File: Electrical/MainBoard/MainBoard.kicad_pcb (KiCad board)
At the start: 4 copper layers, 100 x 86.3 mm, 137 parts, among them J1 SNAP Program, J13 Refl_PCB_Connect, J14 Refl_PCB_Connect, J15 Refl_PCB_Connect, J16 Conn_02x03_Odd_Even, J17 MEM2061-01-188-00-A, J18 Conn_02x02_Odd_Even, J19 Conn_02x03_Odd_Even, J2 3.3V Supply, J20 Conn_02x03_Odd_Even, J21 Conn_02x03_Odd_Even, J22 Conn_02x02_Odd_Even, J23 Conn_02x03_Odd_Even, J24 Conn_01x04, J3 5V Supply, J4 USB_B_Micro, J5 Battery1, J6 Battery1, J7 GPIO1, J8 Conn_02x04_Odd_Even, J9 USB_B_Micro, M1 Motor_DC, M2 Motor_DC, SW1 Reset, SW10 SW_SPST, SW2 5V Bypass, SW3 All Power Switch, SW4 User_Button, SW5 User_Button, SW6 User_Button, SW7 SW_SPST, SW8 SW_SPST, SW9 SW_SPST, U1 PIC32MZ2048EFH144-I/PL, U10 DRV8842PWPR, U11 Quad_Encoder, U12 Quad_Encoder, U13 DRV8842PWPR, U15 M95M01-DFMN6TP, U2 AP2114HA-3.3TRG1, U3 AP2114HA-3.3TRG1, U4 ICM-42688-P, U5 GSF7002DW, U6 GSF7002DW, U7 GSF7002DW, U8 GSF7002DW, U9 MCP2221A-I_SL

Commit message: Add some final touches
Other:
- board text added: "Matthew Sato Engineering Informatics Group Stanford University Robot Control, Rev 0.1 11/25/2023"
- board text removed: "Matthew Sato Engineering Informatics Group Stanford University Robot Control, Rev 0.1 11/24/2023"
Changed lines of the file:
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@@
   (title_block
     (title "Main Robot Board")
+    (date "2023-11-25")
     (rev "0.1")
     (company "satomm@stanford.edu")
@@
     (property "Supplier 2" "")
     (property "Supplier 2 P/N" "")
+    (property "exclude_from_bom" "")
     (property "ki_description" "Mounting Hole without connection")
     (property "ki_keywords" "mounting hole")
-    (attr exclude_from_pos_files)
+    (attr exclude_from_pos_files exclude_from_bom)
     (fp_text reference "H2" (at 0 -4.2) (layer "F.SilkS") hide
         (effects (font (size 1 1) (thickness 0.15)))
@@
     (property "Supplier 2" "")
     (property "Supplier 2 P/N" "")
+    (property "exclude_from_bom" "")
     (property "ki_description" "Mounting Hole without connection")
     (property "ki_keywords" "mounting hole")
-    (attr exclude_from_pos_files)
+    (attr exclude_from_pos_files exclude_from_bom)
     (fp_text reference "H4" (at 0 -4.2) (layer "F.SilkS") hide
         (effects (font (size 1 1) (thickness 0.15)))
@@
     (property "Supplier 2" "")
     (property "Supplier 2 P/N" "")
+    (property "exclude_from_bom" "")
     (property "ki_description" "Mounting Hole without connection")
     (property "ki_keywords" "mounting hole")
-    (attr exclude_from_pos_files)
+    (attr exclude_from_pos_files exclude_from_bom)
     (fp_text reference "H1" (at 0 -4.2) (layer "F.SilkS") hide
         (effects (font (size 1 1) (thickness 0.15)))
@@
     (property "Supplier 2" "")
     (property "Supplier 2 P/N" "")
+    (property "exclude_from_bom" "")
     (property "ki_description" "Mounting Hole without connection")
     (property "ki_keywords" "mounting hole")
-    (attr exclude_from_pos_files)
+    (attr exclude_from_pos_files exclude_from_bom)
     (fp_text reference "H3" (at 0 -4.2) (layer "F.SilkS") hide
         (effects (font (size 1 1) (thickness 0.15)))
@@
     (effects (font (size 1 1) (thickness 0.15)) (justify left bottom))
   )
-  (gr_text "Matthew Sato\nEngineering Informatics Group\nStanford University\nRobot Control, Rev 0.1\n11/24/2023" (at 181.9 152) (layer "F.SilkS")
+  (gr_text "Matthew Sato\nEngineering Informatics Group\nStanford University\nRobot Control, Rev 0.1\n11/25/2023" (at 181.9 152) (layer "F.SilkS")
     (effects (font (size 1 1) (thickness 0.15)) (justify left bottom))
   )

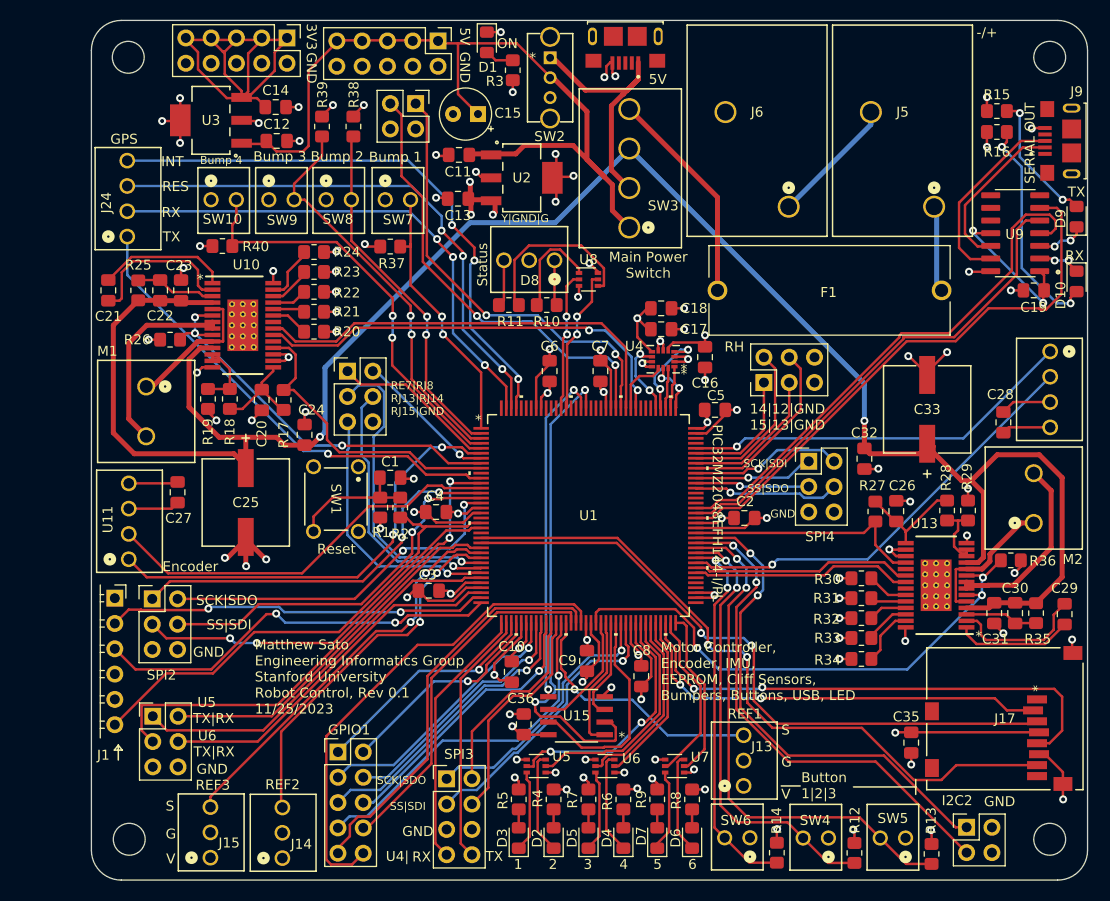
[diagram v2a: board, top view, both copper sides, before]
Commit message: Finish final board design for Rev 0.1 Main board and reflective Sensor. Created Gerbers.
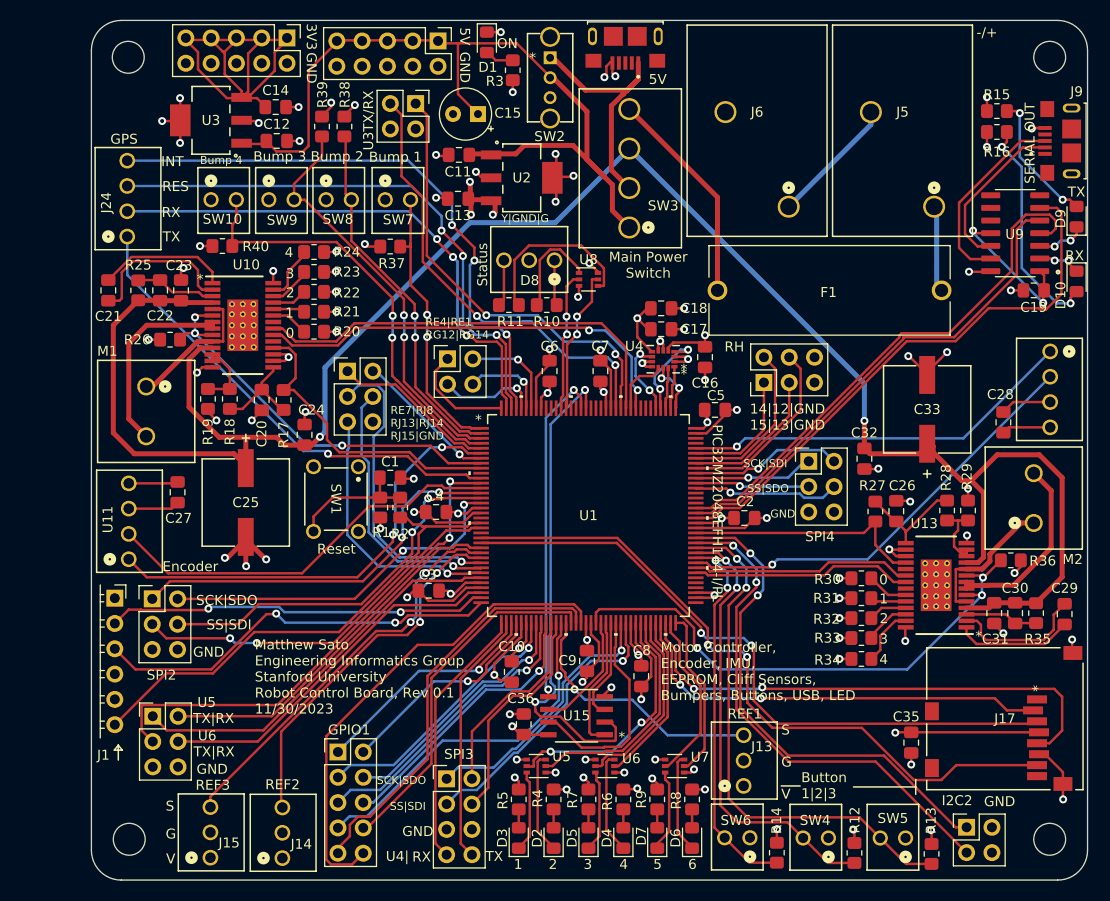
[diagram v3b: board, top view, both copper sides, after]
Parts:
- added J25: Conn_02x02_Odd_Even, Connector_PinHeader_2.54mm:PinHeader_2x02_P2.54mm_Vertical, F.Cu at (201.2, 116.3)
- moved R38 0.90 mm to (190.9, 93.0)
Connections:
- U1 pad 138: unconnected-(U1B-EBID1/PMD1/RE1-Pad138) -> /RE1
- U1 pad 139: unconnected-(U1B-TRD2/SQID2/RG14-Pad139) -> /RG14
- U1 pad 140: unconnected-(U1B-TRD1/SQID1/RG12-Pad140) -> /RG12
- U1 pad 144: unconnected-(U1B-EBID4/AN18/PMD4/RE4-Pad144) -> /RE4
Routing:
- net /RE4: track 0.00 -> 10.9 mm
- net /RG12: track 0.00 -> 10.0 mm, vias 0 -> 1
- net /RE1: track 0.00 -> 9.99 mm, vias 0 -> 1
- net /RG14: track 0.00 -> 8.47 mm, vias 0 -> 1
- net /U2RX: track 52.1 -> 53.5 mm
- net /GPS_INT: track 58.1 -> 59.5 mm
- net /GPS_Reset: track 55.0 -> 56.2 mm
- net /Bump1: track 27.2 -> 28.3 mm
- net /Bump2: track 35.6 -> 36.6 mm
- net /Bump3: track 40.5 -> 41.1 mm
- net /Bump4: track 41.8 -> 42.4 mm
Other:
- board text added: "0"
- board text added: "Matthew Sato Engineering Informatics Group Stanford University Robot Control Board, Rev 0.1 11/30/2023"
- board text added: "RE4|RE1 RG12|RG14"
- board text added: "U3TX/RX"
- board text removed: "Matthew Sato Engineering Informatics Group Stanford University Robot Control, Rev 0.1 11/25/2023"

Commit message: Made V0.2 revisions to Main Board
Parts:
- removed C16: 0.01 uF, Capacitor_SMD:C_0805_2012Metric_Pad1.18x1.45mm_HandSolder
- removed C17: 0.1 uF, Capacitor_SMD:C_0805_2012Metric_Pad1.18x1.45mm_HandSolder
- removed C18: 2.2 uF, Capacitor_SMD:C_0805_2012Metric_Pad1.18x1.45mm_HandSolder
- removed U4: ICM-42688-P, RobotLibrary:LGA14_2P5X3X0P91_TDK-M
- added J26: Conn_02x04_Odd_Even, Connector_PinHeader_2.54mm:PinHeader_2x04_P2.54mm_Vertical, F.Cu at (222.5, 110.4)
- added R47: 0.1R, Resistor_SMD:R_0603_1608Metric_Pad0.98x0.95mm_HandSolder, B.Cu at (170.8, 113.7)
- added R48: 0.05 R, Resistor_SMD:R_0603_1608Metric_Pad0.98x0.95mm_HandSolder, B.Cu at (167.4, 113.7)
- added R49: 0.1R, Resistor_SMD:R_0603_1608Metric_Pad0.98x0.95mm_HandSolder, B.Cu at (260.0, 138.1)
- added R50: 0.05 R, Resistor_SMD:R_0603_1608Metric_Pad0.98x0.95mm_HandSolder, B.Cu at (263.4, 138.1)
- J20: value Conn_02x03_Odd_Even -> Conn_01x06; footprint Connector_PinHeader_2.54mm:PinHeader_2x03_P2.54mm_Vertical -> Connector_Molex:Molex_KK-254_AE-6410-06A_1x06_P2.54mm_Vertical
- R26, R36: value 0.25R -> 0.1R; footprint Resistor_SMD:R_0805_2012Metric_Pad1.20x1.40mm_HandSolder -> Resistor_SMD:R_0603_1608Metric_Pad0.98x0.95mm_HandSolder; moved to B.Cu
- moved J20 2.13 mm to (172.1, 142.4)
- moved R36 1.99 mm to (256.6, 138.1)
- moved R26 1.02 mm to (174.2, 113.7)
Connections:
- J1 pad 1: unconnected-(J1-Pin_1-Pad1) -> Net-(J1-Pin_1)
- J1 pad 2: Net-(J1-Pin_2) -> +3.3V
- J1 pad 3: Net-(J1-Pin_3) -> GND
- J1 pad 4: GND -> Net-(J1-Pin_4)
- J1 pad 5: +3.3V -> Net-(J1-Pin_5)
- J1 pad 6: Net-(J1-Pin_6) -> unconnected-(J1-Pin_6-Pad6)
- J20 pad 2: /SDO2 -> /SS2*
- J20 pad 3: /SS2* -> /SDO2
- R2 pad 1: Net-(J1-Pin_6) -> Net-(J1-Pin_1)
- R26 pad 1: GND -> Net-(R26-Pad1)
- R36 pad 1: GND -> Net-(R36-Pad1)
- U1 pad 20: Net-(J1-Pin_6) -> Net-(J1-Pin_1)
- U1 pad 35: Net-(J1-Pin_2) -> Net-(J1-Pin_5)
- U1 pad 36: Net-(J1-Pin_3) -> Net-(J1-Pin_4)
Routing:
- net Net-(J1-Pin_6): track 49.0 -> 0.00 mm
- net Net-(J1-Pin_5): track 0.00 -> 41.5 mm, vias 0 -> 1
- net Net-(J1-Pin_3): track 41.2 -> 0.00 mm, vias 2 -> 0
- net Net-(J1-Pin_1): track 0.00 -> 40.9 mm, vias 0 -> 1
- net Net-(J1-Pin_4): track 0.00 -> 39.7 mm, vias 0 -> 1
- net Net-(J1-Pin_2): track 38.3 -> 0.00 mm, vias 2 -> 0
- net +3.3V: track 161.9 -> 150.1 mm, vias 42 -> 40
- net GND: track 149.3 -> 138.4 mm, vias 72 -> 66
- net /SS1*: track 5.97 -> 16.2 mm
- net /SDI2: track 38.1 -> 32.2 mm
- net /SCK1: track 5.45 -> 10.1 mm, vias 2 -> 0
- net /SS2*: track 38.6 -> 35.0 mm, vias 2 -> 0
- net /IMU_INT1: track 9.41 -> 6.75 mm, vias 2 -> 0
- net /SDO2: track 36.3 -> 34.1 mm
- net /MotorCurrent2: track 54.1 -> 52.2 mm
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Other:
- board text added: "GND GND"
- board text added: "Matthew Sato, 02/02/2024 Engineering Informatics Group Stanford University Robot Control Board, Rev 0.2"
- board text added: "SCK2"
- board text added: "SDI2"
- board text added: "SDO2"
- board text added: "SS2"
- board text removed: "Matthew Sato Engineering Informatics Group Stanford University Robot Control Board, Rev 0.1 11/30/2023"

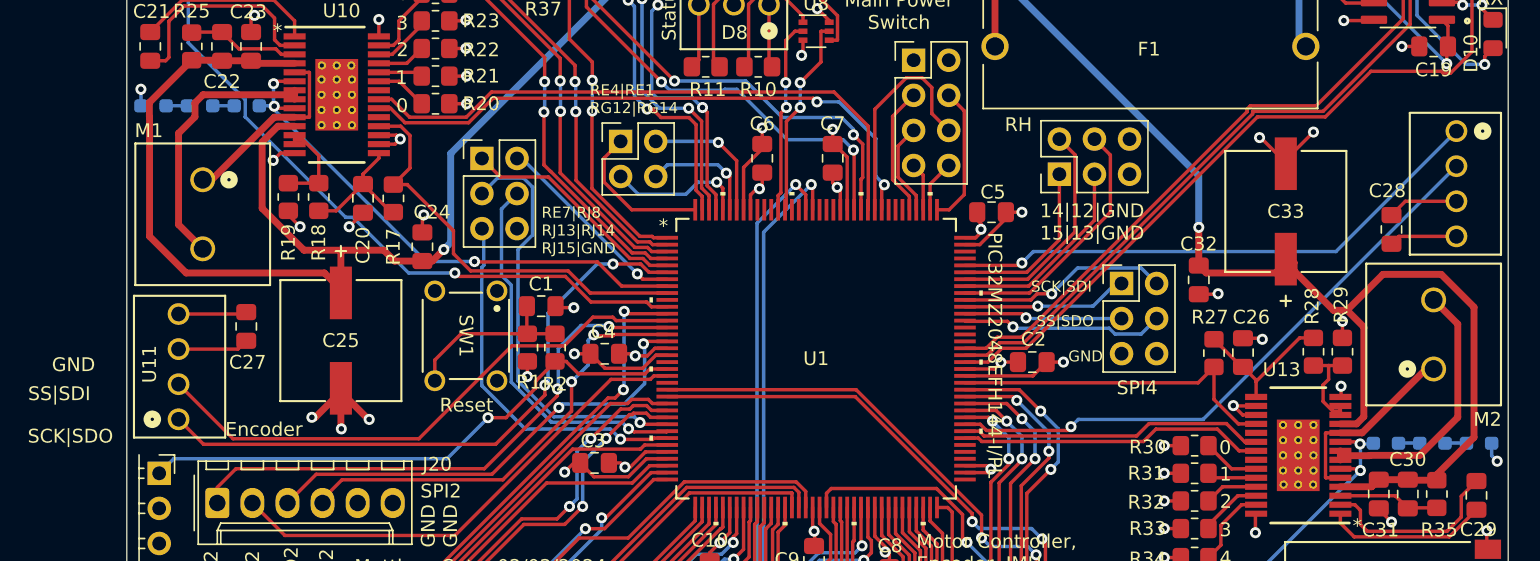
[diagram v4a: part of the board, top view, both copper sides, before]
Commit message: Change molex+terminal block to just 6 position molex for the motor/encoder terminal
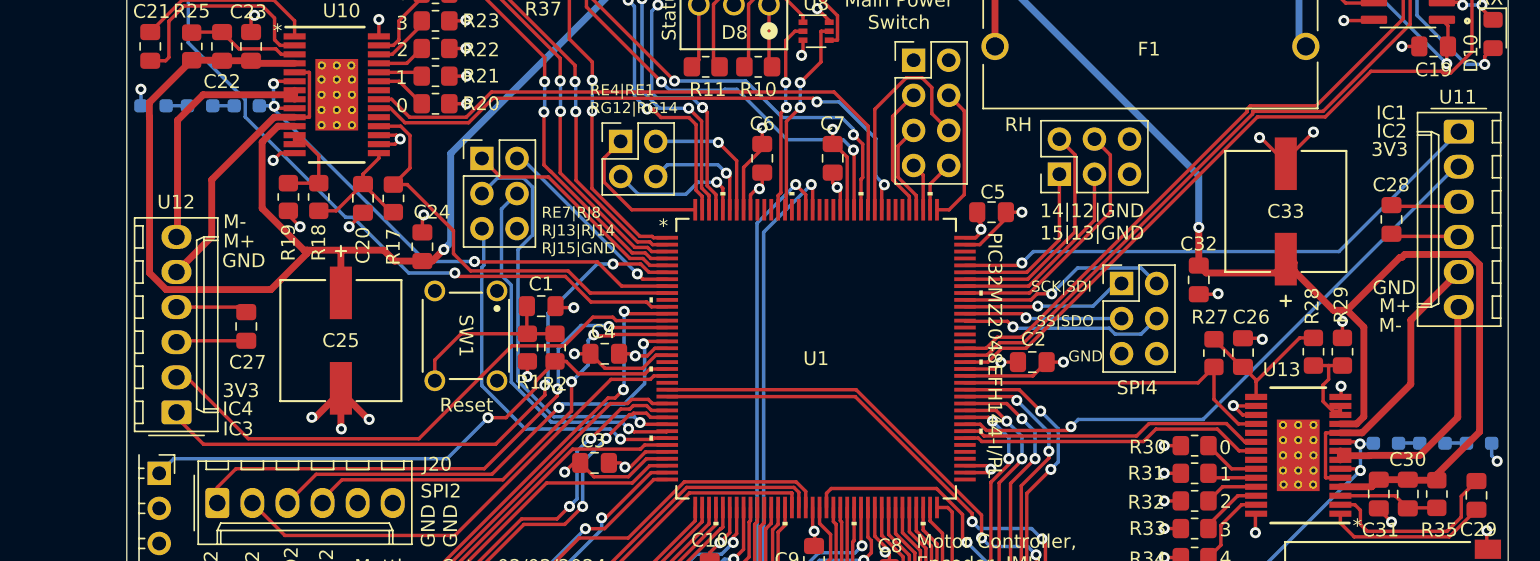
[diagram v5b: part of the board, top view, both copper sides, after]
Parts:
- removed M1, M2: Motor_DC, RobotLibrary:CONN_1890963_PXC
- U11, U12: value Quad_Encoder -> Quad_Encoder_Motor; footprint RobotLibrary:CONN_22-23-2041_MOL -> Connector_Molex:Molex_KK-254_AE-6410-06A_1x06_P2.54mm_Vertical
- moved U11 95.0 mm to (261.9, 115.6), turned to -90 degrees
- moved U12 94.9 mm to (169.1, 135.9), turned to 90 degrees
- moved C28 0.73 mm to (257.1, 121.9)
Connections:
- U10 pad 10: Net-(M1-+) -> Net-(U12-M+)
- U10 pad 5: Net-(M1-+) -> Net-(U12-M+)
- U10 pad 7: Net-(M1--) -> Net-(U12-M-)
- U10 pad 8: Net-(M1--) -> Net-(U12-M-)
- U11 pad 1: /IC3 -> /IC1
- U11 pad 2: /IC4 -> /IC2
- U12 pad 1: /IC1 -> /IC3
- U12 pad 2: /IC2 -> /IC4
- U13 pad 10: Net-(M2-+) -> Net-(U11-M+)
- U13 pad 5: Net-(M2-+) -> Net-(U11-M+)
- U13 pad 7: Net-(M2--) -> Net-(U11-M-)
- U13 pad 8: Net-(M2--) -> Net-(U11-M-)
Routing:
- net Net-(U11-M+): track 0.00 -> 21.5 mm
- net Net-(U12-M+): track 0.00 -> 21.0 mm
- net Net-(M1--): track 19.9 -> 0.00 mm
- net Net-(M2--): track 19.6 -> 0.00 mm
- net Net-(U11-M-): track 0.00 -> 18.4 mm
- net Net-(U12-M-): track 0.00 -> 18.4 mm
- net Net-(M2-+): track 13.5 -> 0.00 mm
- net Net-(M1-+): track 13.2 -> 0.00 mm
- net Vdrive: track 204.4 -> 208.4 mm
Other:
- board text added: "IC1"
- board text added: "IC2"
- board text added: "IC3"
- board text added: "IC4"
- board text added: "M+"
- board text added: "M-"
- board text removed: "Encoder"
